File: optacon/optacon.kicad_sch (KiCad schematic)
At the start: 5 parts, among them J1 Conn_01x22, J2 Conn_01x08, J3 Conn_01x02, U1 HV528, U2 HV528

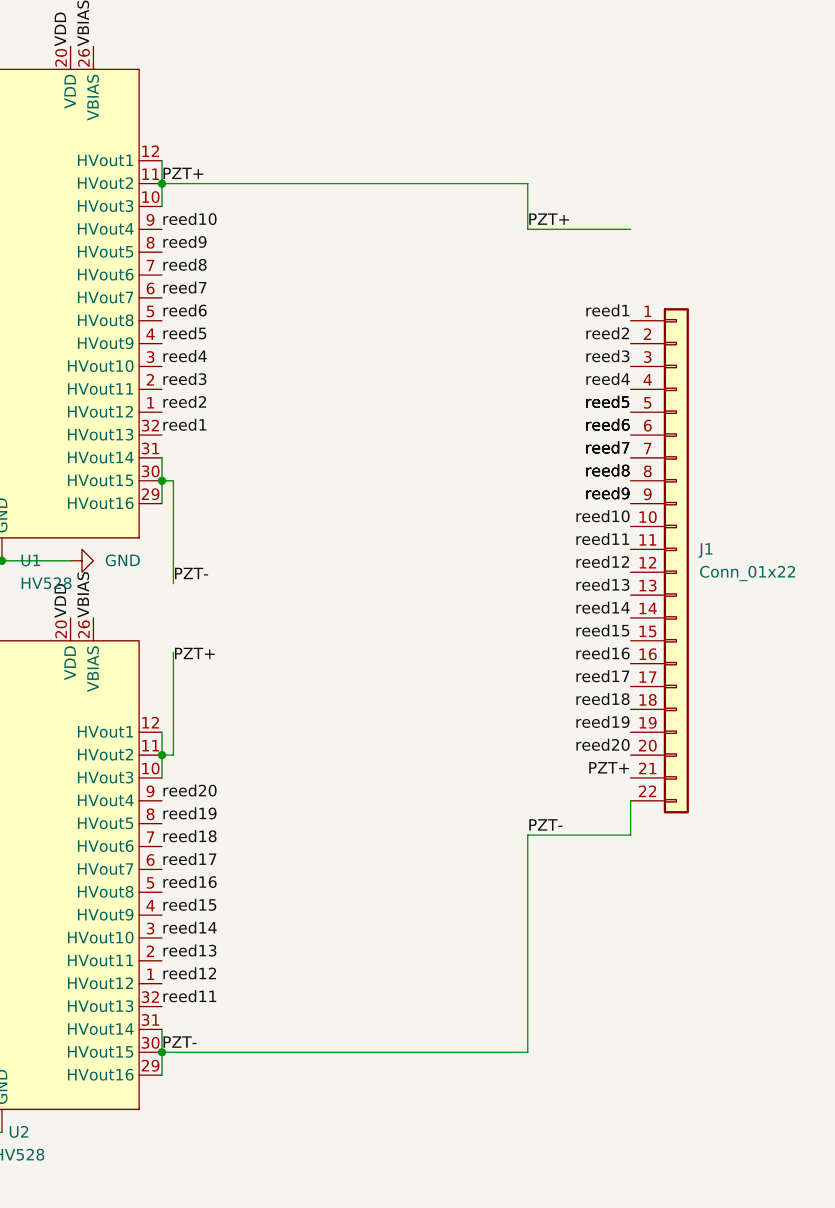
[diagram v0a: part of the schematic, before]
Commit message: wip: piezo footprint, drv2665 symbol
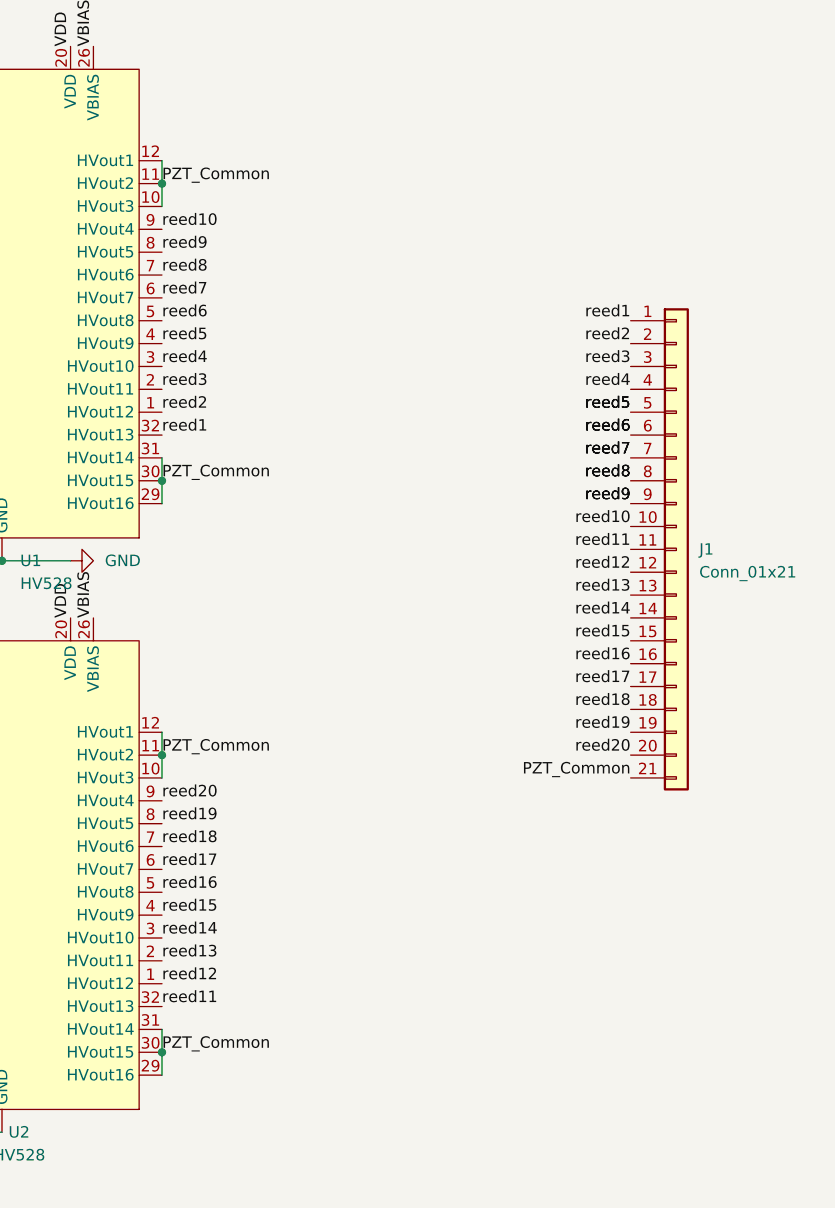
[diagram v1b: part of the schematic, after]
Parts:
- J1: value Conn_01x22 -> Conn_01x21; symbol Connector_Generic:Conn_01x22 -> Connector_Generic:Conn_01x21
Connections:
- net PZT+ renamed PZT_Common
- net PZT_Common: now also U1.29 (HVout16), U1.30 (HVout15), U1.31 (HVout14), U2.29 (HVout16), U2.30 (HVout15), U2.31 (HVout14)
- removed net PZT-: J1.22 (Pin_22), U1.29 (HVout16), U1.30 (HVout15), U1.31 (HVout14), U2.29 (HVout16), U2.30 (HVout15), U2.31 (HVout14)
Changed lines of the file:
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@@
   (no_connect (at 102.87 106.68))
   (no_connect (at 102.87 43.18))
-  (wire (pts (xy 123.19 110.49) (xy 123.19 121.92))
-    (stroke (width 0) (type default) (color 0 0 0 0))
-  )
   (wire (pts (xy 95.25 43.18) (xy 97.79 43.18))
     (stroke (width 0) (type default) (color 0 0 0 0))
@@
     (stroke (width 0) (type default) (color 0 0 0 0))
   )
-  (wire (pts (xy 162.56 154.94) (xy 162.56 130.81))
-    (stroke (width 0) (type default) (color 0 0 0 0))
-  )
-  (wire (pts (xy 121.92 91.44) (xy 123.19 91.44))
-    (stroke (width 0) (type default) (color 0 0 0 0))
-  )
   (wire (pts (xy 76.2 63.5) (xy 90.17 63.5))
     (stroke (width 0) (type default) (color 0 0 0 0))
   )
-  (wire (pts (xy 173.99 127) (xy 173.99 130.81))
-    (stroke (width 0) (type default) (color 0 0 0 0))
-  )
-  (wire (pts (xy 121.92 58.42) (xy 162.56 58.42))
-    (stroke (width 0) (type default) (color 0 0 0 0))
-  )
   (wire (pts (xy 40.64 60.96) (xy 78.74 60.96))
     (stroke (width 0) (type default) (color 0 0 0 0))
@@
     (stroke (width 0) (type default) (color 0 0 0 0))
   )
-  (wire (pts (xy 121.92 154.94) (xy 162.56 154.94))
-    (stroke (width 0) (type default) (color 0 0 0 0))
-  )
-  (wire (pts (xy 162.56 63.5) (xy 173.99 63.5))
-    (stroke (width 0) (type default) (color 0 0 0 0))
-  )
   (wire (pts (xy 78.74 60.96) (xy 78.74 124.46))
     (stroke (width 0) (type default) (color 0 0 0 0))
@@
     (stroke (width 0) (type default) (color 0 0 0 0))
   )
-  (wire (pts (xy 121.92 121.92) (xy 123.19 121.92))
-    (stroke (width 0) (type default) (color 0 0 0 0))
-  )
   (wire (pts (xy 121.92 55.88) (xy 121.92 58.42))
     (stroke (width 0) (type default) (color 0 0 0 0))
@@
     (stroke (width 0) (type default) (color 0 0 0 0))
   )
-  (wire (pts (xy 123.19 91.44) (xy 123.19 102.87))
-    (stroke (width 0) (type default) (color 0 0 0 0))
-  )
   (wire (pts (xy 80.01 58.42) (xy 80.01 121.92))
     (stroke (width 0) (type default) (color 0 0 0 0))
@@
     (stroke (width 0) (type default) (color 0 0 0 0))
   )
-  (wire (pts (xy 162.56 130.81) (xy 173.99 130.81))
-    (stroke (width 0) (type default) (color 0 0 0 0))
-  )
   (wire (pts (xy 121.92 119.38) (xy 121.92 121.92))
     (stroke (width 0) (type default) (color 0 0 0 0))
@@
     (stroke (width 0) (type default) (color 0 0 0 0))
   )
-  (wire (pts (xy 162.56 58.42) (xy 162.56 63.5))
-    (stroke (width 0) (type default) (color 0 0 0 0))
-  )
   (label "reed6" (at 121.92 73.66 0)
     (effects (font (size 1.27 1.27)) (justify left bottom))
@@
     (effects (font (size 1.27 1.27)) (justify left bottom))
   )
-  (label "PZT-" (at 123.19 102.87 0)
-    (effects (font (size 1.27 1.27)) (justify left bottom))
-  )
-  (label "PZT+" (at 162.56 63.5 0)
+  (label "PZT_Common" (at 121.92 121.92 0)
     (effects (font (size 1.27 1.27)) (justify left bottom))
   )
@@
     (effects (font (size 1.27 1.27)) (justify right bottom))
   )
-  (label "PZT+" (at 121.92 58.42 0)
+  (label "PZT_Common" (at 121.92 58.42 0)
     (effects (font (size 1.27 1.27)) (justify left bottom))
   )
@@
     (effects (font (size 1.27 1.27)) (justify right bottom))
   )
-  (label "PZT-" (at 121.92 154.94 0)
-    (effects (font (size 1.27 1.27)) (justify left bottom))
-  )
   (label "reed8" (at 173.99 91.44 180)
     (effects (font (size 1.27 1.27)) (justify right bottom))
   )
-  (label "PZT+" (at 123.19 111.76 0)
-    (effects (font (size 1.27 1.27)) (justify left bottom))
-  )
   (label "reed15" (at 121.92 139.7 0)
     (effects (font (size 1.27 1.27)) (justify left bottom))
@@
     (effects (font (size 1.27 1.27)) (justify right bottom))
   )
-  (label "PZT-" (at 162.56 130.81 0)
+  (label "PZT_Common" (at 121.92 91.44 0)
     (effects (font (size 1.27 1.27)) (justify left bottom))
   )
@@
     (effects (font (size 1.27 1.27)) (justify left bottom))
   )
+  (label "PZT_Common" (at 121.92 154.94 0)
+    (effects (font (size 1.27 1.27)) (justify left bottom))
+  )
   (label "DOUT" (at 40.64 129.54 180)
     (effects (font (size 1.27 1.27)) (justify right bottom))
   )
-  (label "PZT+" (at 173.99 124.46 180)
+  (label "PZT_Common" (at 173.99 124.46 180)
     (effects (font (size 1.27 1.27)) (justify right bottom))
   )
@@
     (pin "9")
   )
-  (symbol (lib_id "Connector_Generic:Conn_01x22") (at 179.07 99.06 0) (unit 1)
+  (symbol (lib_id "Connector_Generic:Conn_01x21") (at 179.07 99.06 0) (unit 1)
     (in_bom yes) (on_board yes) (fields_autoplaced)
     (property "Reference" "J1" (id 0) (at 181.61 99.0599 0)
       (effects (font (size 1.27 1.27)) (justify left))
     )
-    (property "Value" "Conn_01x22" (id 1) (at 181.61 101.5999 0)
+    (property "Value" "Conn_01x21" (id 1) (at 181.61 101.5999 0)
       (effects (font (size 1.27 1.27)) (justify left))
     )
@@
     (pin "20")
     (pin "21")
-    (pin "22")
     (pin "3")
     (pin "4")
@@
     )
     (path "/25b5f915-60e0-47e9-bb11-9070f81cf494"
-      (reference "J1") (unit 1) (value "Conn_01x22") (footprint "microchip_hv:piezox20")
+      (reference "J1") (unit 1) (value "Conn_01x21") (footprint "microchip_hv:piezox20")
     )
     (path "/6409c081-55e6-45e9-87cb-465a8b85bf58"

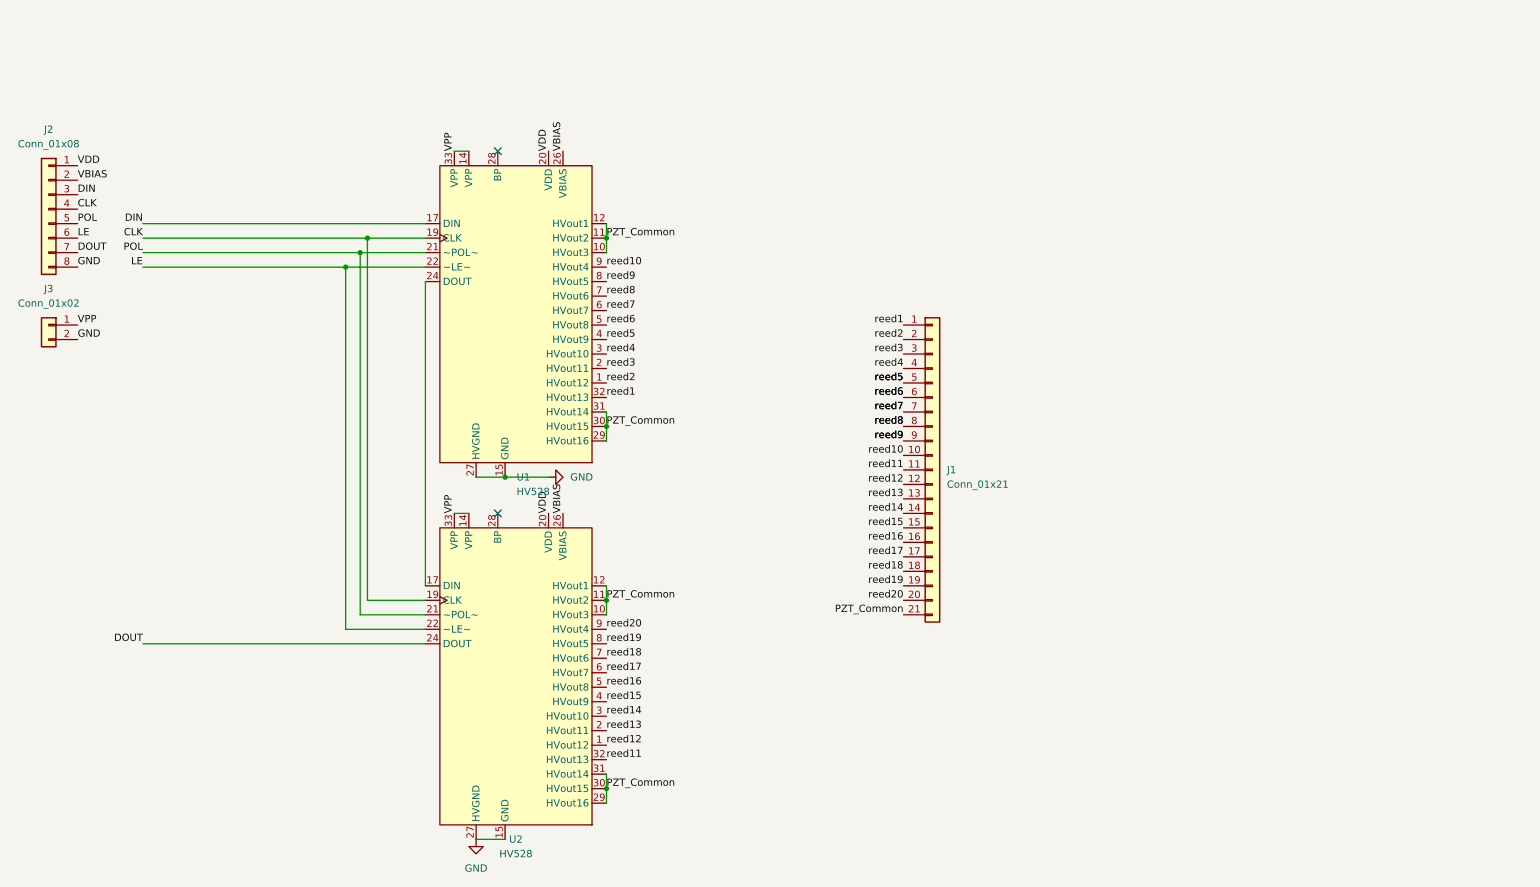
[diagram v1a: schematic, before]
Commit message: drv2665 subsheet
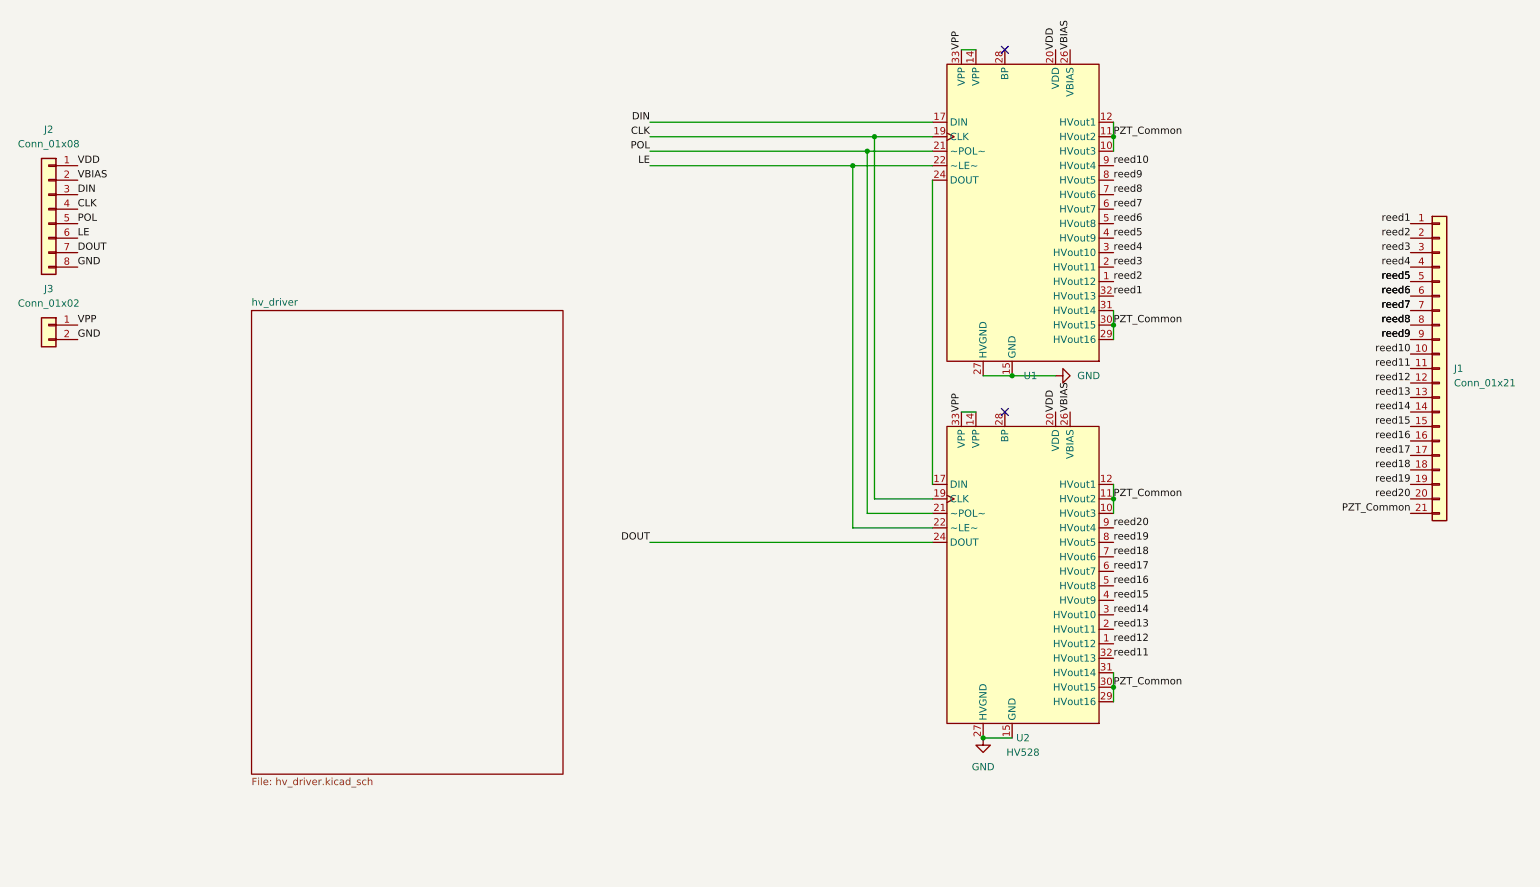
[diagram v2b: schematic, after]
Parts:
- U1: value HV528 -> (none); footprint Package_DFN_QFN:HVQFN-32-1EP_5x5mm_P0.5mm_EP3.1x3.1mm -> (none)
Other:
- added sheet hv_driver (hv_driver.kicad_sch)
- moved on the sheet: J1, U1, U2

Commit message: schematic, footprints
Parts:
- removed J2: Conn_01x08, Connector_PinHeader_2.54mm:PinHeader_1x08_P2.54mm_Vertical, symbol Connector_Generic:Conn_01x08
- removed J3: Conn_01x02, Connector_PinHeader_2.54mm:PinHeader_1x02_P2.54mm_Vertical, symbol Connector_Generic:Conn_01x02
- added D1: D, Diode_SMD:D_0805_2012Metric, symbol Device:D
- added J1: (no value), symbol Connector_Generic:Conn_01x12
- U1: value (none) -> HV528; footprint (none) -> Package_DFN_QFN:HVQFN-32-1EP_5x5mm_P0.5mm_EP3.1x3.1mm
- renumbered J1 to piezo1
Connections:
- net CLK: now also J1.4 (Pin_4)
- net DIN: now also J1.3 (Pin_3)
- net DOUT: now also J1.7 (Pin_7)
- net GND: now also J1.8 (Pin_8)
- net LE: now also J1.6 (Pin_6)
- net POL: now also J1.5 (Pin_5)
- net VBIAS: now also J1.2 (Pin_2)
- net VDD: now also D1.2 (A), J1.1 (Pin_1)
- net VPP: now also D1.1 (K)
- new net IN+: J1.9 (Pin_9)
- new net REG: J1.12 (Pin_12)
- new net SCL: J1.10 (Pin_10)
- new net SDA: J1.11 (Pin_11)
- no-connect marks 2 -> 4
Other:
- sheet hv_driver ports: added IN+, IN-, OUT+, OUT-, REG, SCL, SDA, VDD; removed none
